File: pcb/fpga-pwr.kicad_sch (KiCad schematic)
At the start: 3 parts

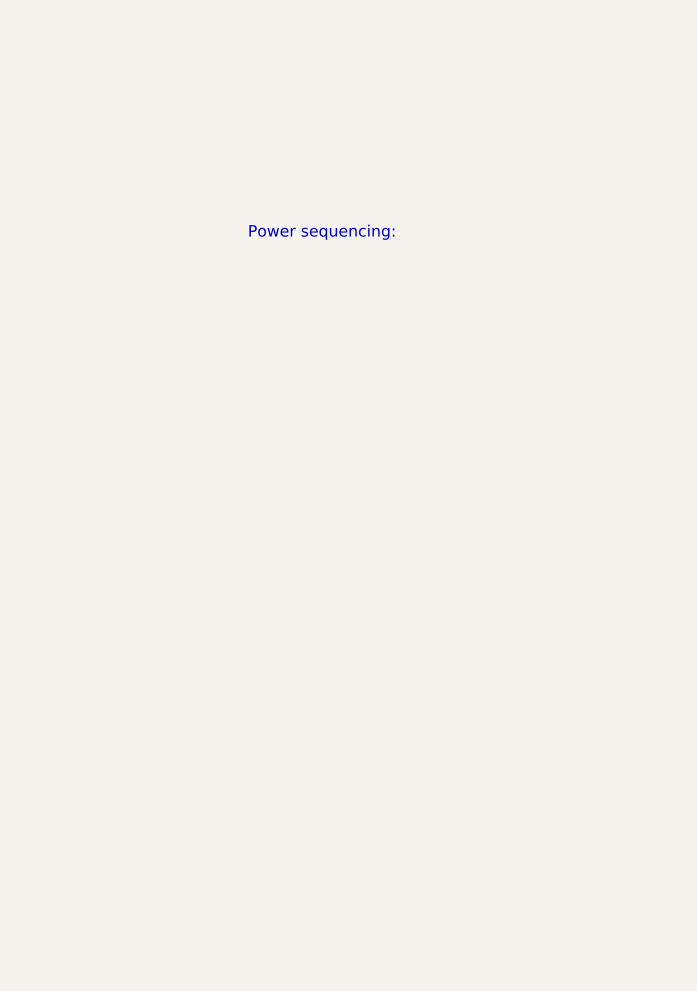
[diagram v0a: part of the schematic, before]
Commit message: current sense, fpga power sequencing
plus restructuring files
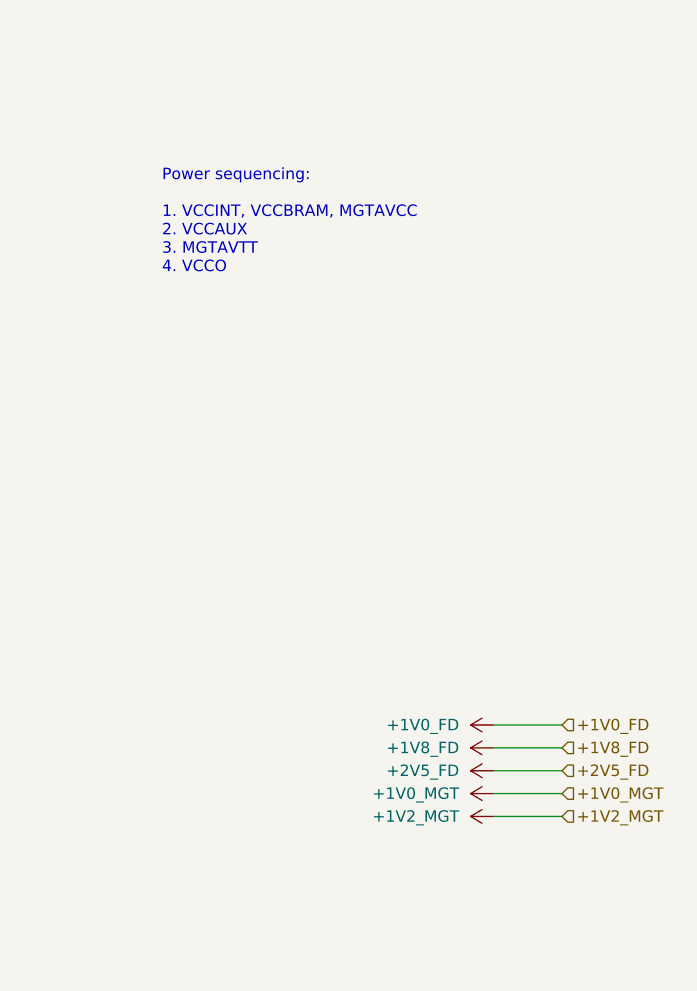
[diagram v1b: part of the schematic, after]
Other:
- note added: "Power sequencing: 1. VCCINT, VCCBRAM, MGTAVCC 2. VCCAUX 3. MGTAVTT 4. VCCO"
- note removed: "Power sequencing:"

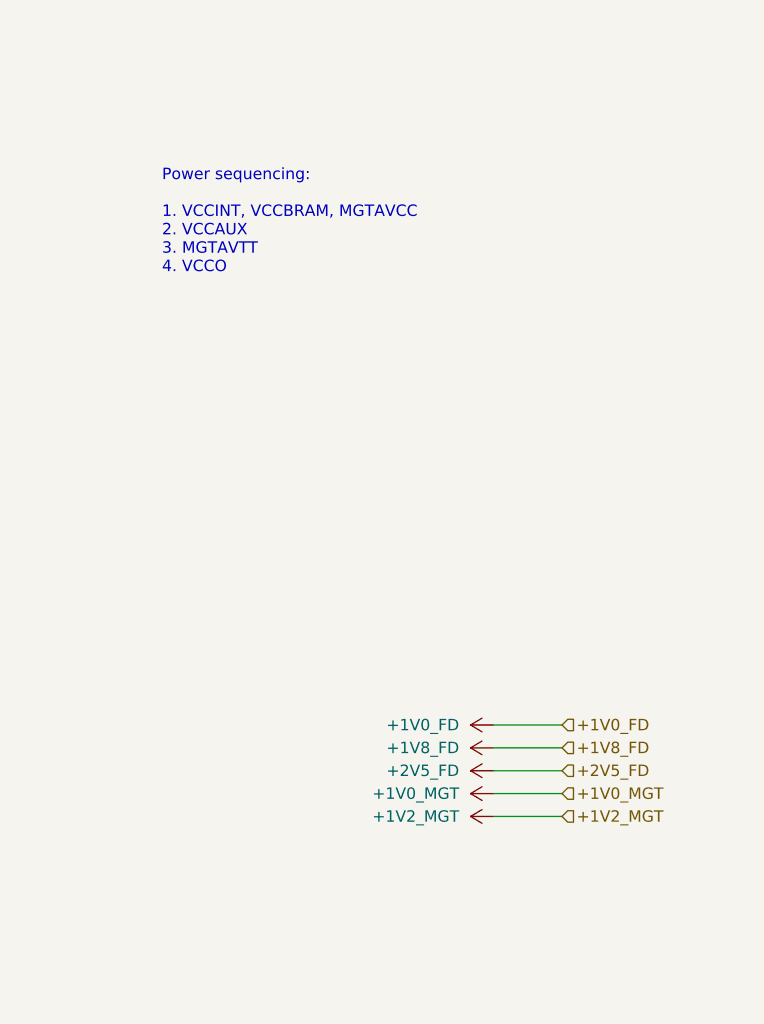
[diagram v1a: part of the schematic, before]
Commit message: add sensors, hierarchical changes
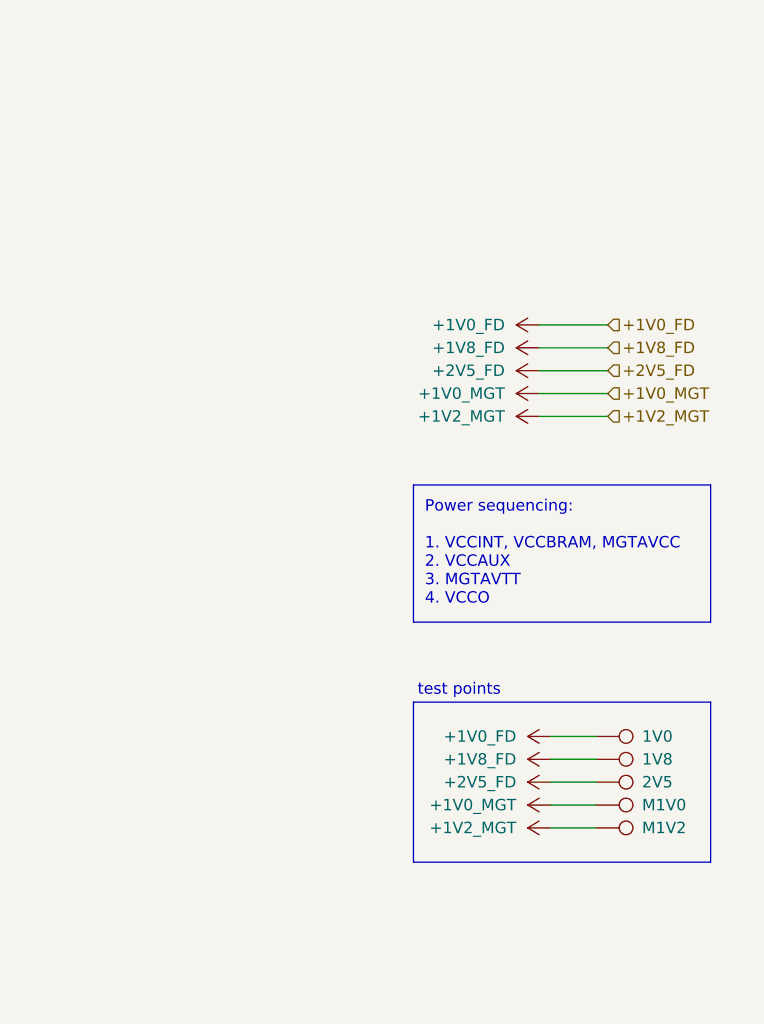
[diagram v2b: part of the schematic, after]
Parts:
- added 1V0, 1V8, 2V5, M1V0, M1V2: TestPoint, symbol Connector:TestPoint
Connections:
- net +1V0_FD: now also 1V0.1
- net +1V0_MGT: now also M1V0.1
- net +1V2_MGT: now also M1V2.1
- net +1V8_FD: now also 1V8.1
- net +2V5_FD: now also 2V5.1
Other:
- note added: "test points"

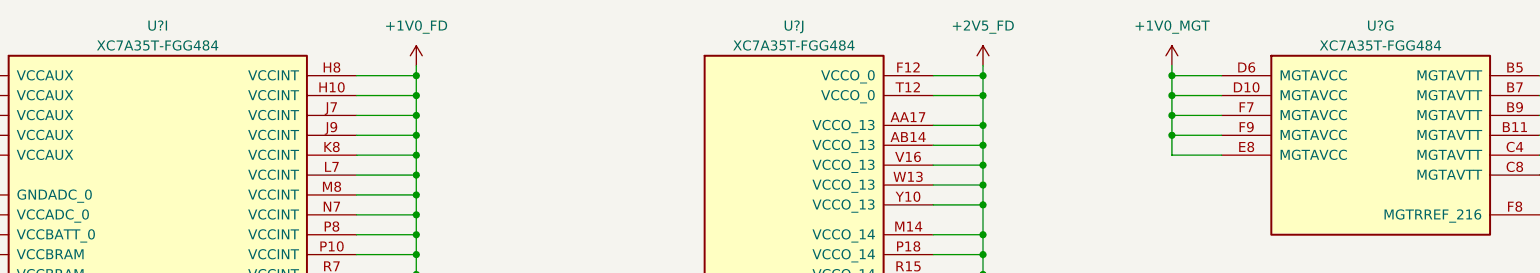
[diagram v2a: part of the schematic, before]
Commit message: addl. updates to power hierarchy
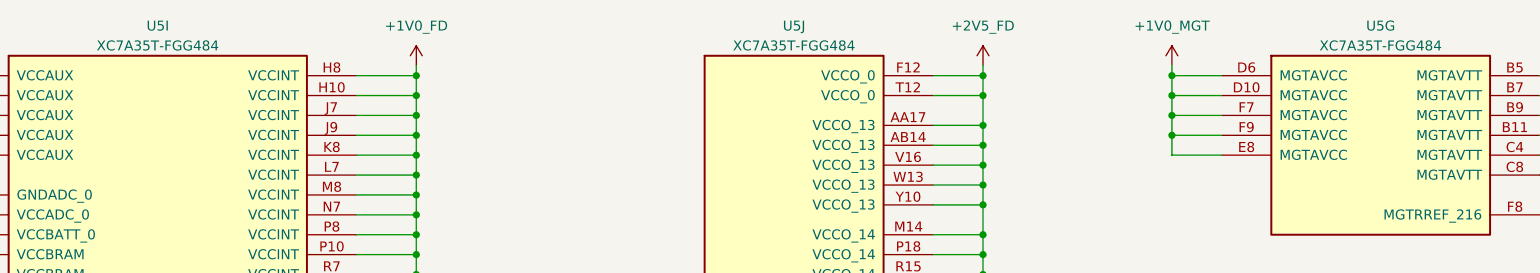
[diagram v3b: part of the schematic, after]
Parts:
- 1V0, 1V8, 2V5, M1V0, M1V2: footprint (none) -> TestPoint:TestPoint_Pad_D1.0mm
- gave numbers to parts that had none: 1
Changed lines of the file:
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@@
 			)
 		)
-		(property "Footprint" ""
+		(property "Footprint" "TestPoint:TestPoint_Pad_D1.0mm"
 			(at 265.43 151.13 0)
 			(effects
@@
 		(dnp no)
 		(fields_autoplaced yes)
-		(property "Reference" "#PWR017"
+		(property "Reference" "#PWR013"
 			(at 100.33 184.15 0)
 			(effects
@@
 			(project "RPi-HwAB-1"
 				(path "/e63e39d7-6ac0-4ffd-8aa3-1841a4541b55/0b49ba4a-009a-499f-8ab2-0eb031fe8200"
-					(reference "#PWR017")
+					(reference "#PWR013")
 					(unit 1)
 				)
@@
 		(dnp no)
 		(fields_autoplaced yes)
-		(property "Reference" "#PWR014"
+		(property "Reference" "#PWR015"
 			(at 196.85 31.75 0)
 			(effects
@@
 			(project "RPi-HwAB-1"
 				(path "/e63e39d7-6ac0-4ffd-8aa3-1841a4541b55/0b49ba4a-009a-499f-8ab2-0eb031fe8200"
-					(reference "#PWR014")
+					(reference "#PWR015")
 					(unit 1)
 				)
@@
 			)
 		)
-		(property "Footprint" ""
+		(property "Footprint" "TestPoint:TestPoint_Pad_D1.0mm"
 			(at 265.43 156.21 0)
 			(effects
@@
 			)
 		)
-		(property "Footprint" ""
+		(property "Footprint" "TestPoint:TestPoint_Pad_D1.0mm"
 			(at 265.43 161.29 0)
 			(effects
@@
 		(dnp no)
 		(fields_autoplaced yes)
-		(property "Reference" "#PWR018"
+		(property "Reference" "#PWR014"
 			(at 172.72 31.75 0)
 			(effects
@@
 			(project "RPi-HwAB-1"
 				(path "/e63e39d7-6ac0-4ffd-8aa3-1841a4541b55/0b49ba4a-009a-499f-8ab2-0eb031fe8200"
-					(reference "#PWR018")
+					(reference "#PWR014")
 					(unit 1)
 				)
@@
 		(dnp no)
 		(fields_autoplaced yes)
-		(property "Reference" "U?"
+		(property "Reference" "U5"
 			(at 223.52 22.86 0)
 			(effects
@@
 			(project "RPi-HwAB-1"
 				(path "/e63e39d7-6ac0-4ffd-8aa3-1841a4541b55/0b49ba4a-009a-499f-8ab2-0eb031fe8200"
-					(reference "U?")
+					(reference "U5")
 					(unit 7)
 				)
@@
 		(dnp no)
 		(fields_autoplaced yes)
-		(property "Reference" "#PWR020"
+		(property "Reference" "#PWR017"
 			(at 262.89 100.33 0)
 			(effects
@@
 			(project "RPi-HwAB-1"
 				(path "/e63e39d7-6ac0-4ffd-8aa3-1841a4541b55/0b49ba4a-009a-499f-8ab2-0eb031fe8200"
-					(reference "#PWR020")
+					(reference "#PWR017")
 					(unit 1)
 				)
@@
 			)
 		)
-		(property "Footprint" ""
+		(property "Footprint" "TestPoint:TestPoint_Pad_D1.0mm"
 			(at 265.43 158.75 0)
 			(effects
@@
 		(dnp no)
 		(fields_autoplaced yes)
-		(property "Reference" "#PWR03"
+		(property "Reference" "#PWR021"
 			(at 262.89 110.49 0)
 			(effects
@@
 			(project "RPi-HwAB-1"
 				(path "/e63e39d7-6ac0-4ffd-8aa3-1841a4541b55/0b49ba4a-009a-499f-8ab2-0eb031fe8200"
-					(reference "#PWR03")
+					(reference "#PWR021")
 					(unit 1)
 				)
@@
 		(dnp no)
 		(fields_autoplaced yes)
-		(property "Reference" "#PWR019"
+		(property "Reference" "#PWR020"
 			(at 262.89 107.95 0)
 			(effects
@@
 			(project "RPi-HwAB-1"
 				(path "/e63e39d7-6ac0-4ffd-8aa3-1841a4541b55/0b49ba4a-009a-499f-8ab2-0eb031fe8200"
-					(reference "#PWR019")
+					(reference "#PWR020")
 					(unit 1)
 				)
@@
 		(dnp no)
 		(fields_autoplaced yes)
-		(property "Reference" "#PWR010"
+		(property "Reference" "#PWR022"
 			(at 264.16 146.05 0)
 			(effects
@@
 			(project "RPi-HwAB-1"
 				(path "/e63e39d7-6ac0-4ffd-8aa3-1841a4541b55/0b49ba4a-009a-499f-8ab2-0eb031fe8200"
-					(reference "#PWR010")
+					(reference "#PWR022")
 					(unit 1)
 				)
@@
 		(dnp no)
 		(fields_autoplaced yes)
-		(property "Reference" "#PWR015"
+		(property "Reference" "#PWR016"
 			(at 250.19 31.75 0)
 			(effects
@@
 			(project "RPi-HwAB-1"
 				(path "/e63e39d7-6ac0-4ffd-8aa3-1841a4541b55/0b49ba4a-009a-499f-8ab2-0eb031fe8200"
-					(reference "#PWR015")
+					(reference "#PWR016")
 					(unit 1)
 				)
@@
 		(dnp no)
 		(fields_autoplaced yes)
-		(property "Reference" "#PWR011"
+		(property "Reference" "#PWR012"
 			(at 100.33 31.75 0)
 			(effects
@@
 			(project ""
 				(path "/e63e39d7-6ac0-4ffd-8aa3-1841a4541b55/0b49ba4a-009a-499f-8ab2-0eb031fe8200"
-					(reference "#PWR011")
+					(reference "#PWR012")
 					(unit 1)
 				)
@@
 		(dnp no)
 		(fields_autoplaced yes)
-		(property "Reference" "#PWR021"
+		(property "Reference" "#PWR018"
 			(at 262.89 102.87 0)
 			(effects
@@
 			(project "RPi-HwAB-1"
 				(path "/e63e39d7-6ac0-4ffd-8aa3-1841a4541b55/0b49ba4a-009a-499f-8ab2-0eb031fe8200"
-					(reference "#PWR021")
+					(reference "#PWR018")
 					(unit 1)
 				)
@@
 		(dnp no)
 		(fields_autoplaced yes)
-		(property "Reference" "#PWR022"
+		(property "Reference" "#PWR019"
 			(at 262.89 105.41 0)
 			(effects
@@
 			(project "RPi-HwAB-1"
 				(path "/e63e39d7-6ac0-4ffd-8aa3-1841a4541b55/0b49ba4a-009a-499f-8ab2-0eb031fe8200"
-					(reference "#PWR022")
+					(reference "#PWR019")
 					(unit 1)
 				)
@@
 		(on_board yes)
 		(dnp no)
-		(property "Reference" "#PWR012"
+		(property "Reference" "#PWR010"
 			(at 27.94 31.75 0)
 			(effects
@@
 			(project ""
 				(path "/e63e39d7-6ac0-4ffd-8aa3-1841a4541b55/0b49ba4a-009a-499f-8ab2-0eb031fe8200"
-					(reference "#PWR012")
+					(reference "#PWR010")
 					(unit 1)
 				)
@@
 		(dnp no)
 		(fields_autoplaced yes)
-		(property "Reference" "U?"
+		(property "Reference" "U5"
 			(at 148.59 22.86 0)
 			(effects
@@
 			(project "RPi-HwAB-1"
 				(path "/e63e39d7-6ac0-4ffd-8aa3-1841a4541b55/0b49ba4a-009a-499f-8ab2-0eb031fe8200"
-					(reference "U?")
+					(reference "U5")
 					(unit 10)
 				)
@@
 		(dnp no)
 		(fields_autoplaced yes)
-		(property "Reference" "#PWR016"
+		(property "Reference" "#PWR011"
 			(at 34.29 184.15 0)
 			(effects
@@
 			(project ""
 				(path "/e63e39d7-6ac0-4ffd-8aa3-1841a4541b55/0b49ba4a-009a-499f-8ab2-0eb031fe8200"
-					(reference "#PWR016")
+					(reference "#PWR011")
 					(unit 1)
 				)
@@
 		(dnp no)
 		(fields_autoplaced yes)
-		(property "Reference" "U?"
+		(property "Reference" "U5"
 			(at 67.31 22.86 0)
 			(effects
@@
 			(project "RPi-HwAB-1"
 				(path "/e63e39d7-6ac0-4ffd-8aa3-1841a4541b55/0b49ba4a-009a-499f-8ab2-0eb031fe8200"
-					(reference "U?")
+					(reference "U5")
 					(unit 9)
 				)
@@
 		(dnp no)
 		(fields_autoplaced yes)
-		(property "Reference" "#PWR013"
+		(property "Reference" "#PWR09"
 			(at 17.78 54.61 0)
 			(effects
@@
 			(project "RPi-HwAB-1"
 				(path "/e63e39d7-6ac0-4ffd-8aa3-1841a4541b55/0b49ba4a-009a-499f-8ab2-0eb031fe8200"
-					(reference "#PWR013")
+					(reference "#PWR09")
 					(unit 1)
 				)
@@
 			)
 		)
-		(property "Footprint" ""
+		(property "Footprint" "TestPoint:TestPoint_Pad_D1.0mm"
 			(at 265.43 153.67 0)
 			(effects

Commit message: added power sequencing through raspi gpio
additionally defined sensors
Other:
- company: (none) -> Andre S Winkel
- title: (none) -> RPi HwAB HAT+
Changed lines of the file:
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@@
 	(generator_version "9.0")
 	(paper "A4")
+	(title_block
+		(title "RPi HwAB HAT+")
+		(date "2025-08-23")
+		(rev "01")
+		(company "Andre S Winkel")
+	)
 	(rectangle
 		(start 245.11 142.24)

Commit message: quick edits to hierarchy
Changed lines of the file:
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@@
 	)
 	(junction
-		(at 17.78 52.07)
+		(at 20.32 52.07)
 		(diameter 0)
 		(color 0 0 0 0)
@@
 	)
 	(junction
-		(at 17.78 54.61)
+		(at 20.32 54.61)
 		(diameter 0)
 		(color 0 0 0 0)
@@
 	(wire
 		(pts
-			(xy 17.78 52.07) (xy 41.91 52.07)
+			(xy 20.32 52.07) (xy 41.91 52.07)
 		)
 		(stroke
@@
 	(wire
 		(pts
-			(xy 17.78 54.61) (xy 17.78 52.07)
+			(xy 20.32 54.61) (xy 20.32 52.07)
 		)
 		(stroke
@@
 	(wire
 		(pts
-			(xy 17.78 52.07) (xy 17.78 50.8)
+			(xy 20.32 52.07) (xy 20.32 50.8)
 		)
 		(stroke
@@
 	(wire
 		(pts
-			(xy 17.78 57.15) (xy 41.91 57.15)
+			(xy 20.32 57.15) (xy 41.91 57.15)
 		)
 		(stroke
@@
 	(wire
 		(pts
-			(xy 17.78 57.15) (xy 17.78 54.61)
+			(xy 20.32 57.15) (xy 20.32 54.61)
 		)
 		(stroke
@@
 	(wire
 		(pts
-			(xy 17.78 54.61) (xy 41.91 54.61)
+			(xy 20.32 54.61) (xy 41.91 54.61)
 		)
 		(stroke
@@
 	(symbol
 		(lib_id "power:+1V0")
-		(at 17.78 50.8 0)
+		(at 20.32 50.8 0)
 		(unit 1)
 		(exclude_from_sim no)
@@
 		(fields_autoplaced yes)
 		(property "Reference" "#PWR09"
-			(at 17.78 54.61 0)
+			(at 20.32 54.61 0)
 			(effects
 				(font
@@
 		)
 		(property "Value" "+1V0_FD"
-			(at 17.78 45.72 0)
+			(at 20.32 45.72 0)
 			(effects
 				(font
@@
 		)
 		(property "Footprint" ""
-			(at 17.78 50.8 0)
+			(at 20.32 50.8 0)
 			(effects
 				(font
@@
 		)
 		(property "Datasheet" ""
-			(at 17.78 50.8 0)
+			(at 20.32 50.8 0)
 			(effects
 				(font
@@
 		)
 		(property "Description" "Power symbol creates a global label with name \"+1V0\""
-			(at 17.78 50.8 0)
+			(at 20.32 50.8 0)
 			(effects
 				(font

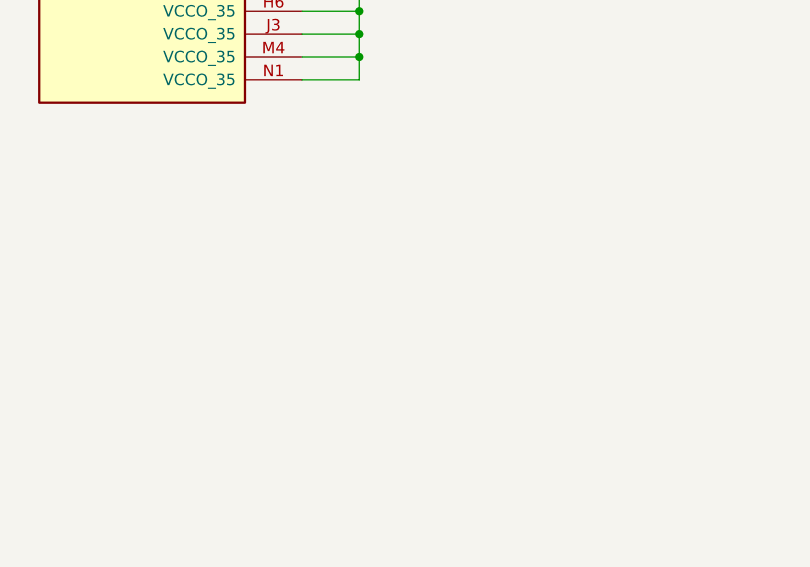
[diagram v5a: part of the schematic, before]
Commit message: defined pcie diff. connections
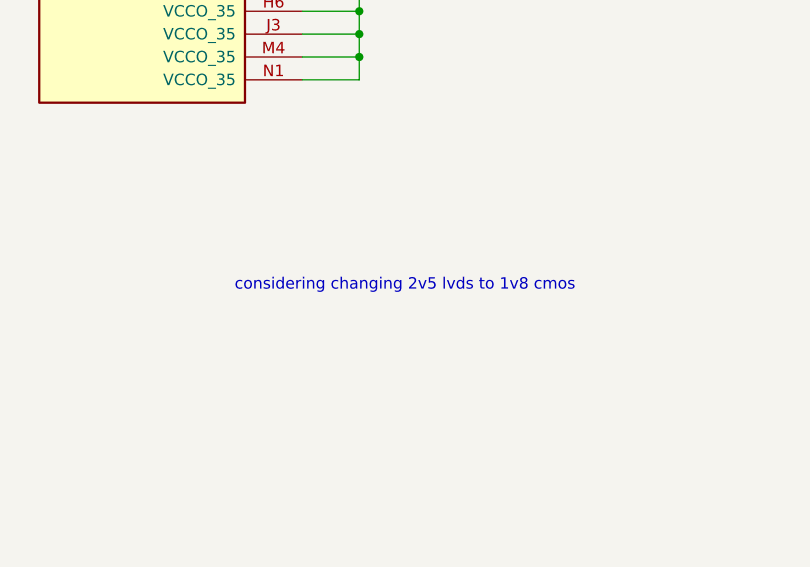
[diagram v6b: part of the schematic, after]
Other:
- note added: "considering changing 2v5 lvds to 1v8 cmos"
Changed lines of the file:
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@@
+		)
+	)
+	(text "considering changing 2v5 lvds to 1v8 cmos"
+		(exclude_from_sim no)
+		(at 177.8 151.13 0)
+		(effects
+			(font
+				(size 1.27 1.27)
+			)
 		)
 	)
